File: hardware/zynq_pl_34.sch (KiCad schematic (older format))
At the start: 1 part

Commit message: Added a few Todos.
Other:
- note added: "TODO: VCCO(AFAIK 1,8 V), is VREF needed for this single ended signals?"
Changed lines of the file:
@@
 Wire Wire Line
 	5250 2200 4800 2200
+Text Notes 1650 1350 0    60   ~ 0
+TODO: VCCO(AFAIK 1,8 V), is VREF needed for this single ended signals?
 $EndSCHEMATC

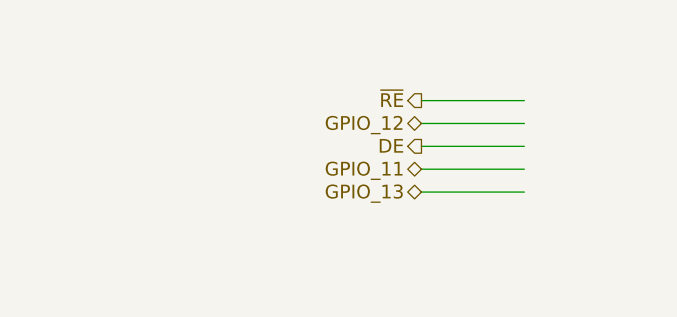
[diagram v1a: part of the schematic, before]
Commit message: Added decoupling Capacitors for the Zynq. Also added the 2,5 V Power supply.
The 2,5 V supply was implemented as LDO and is sourced by the 3,3 V Line.
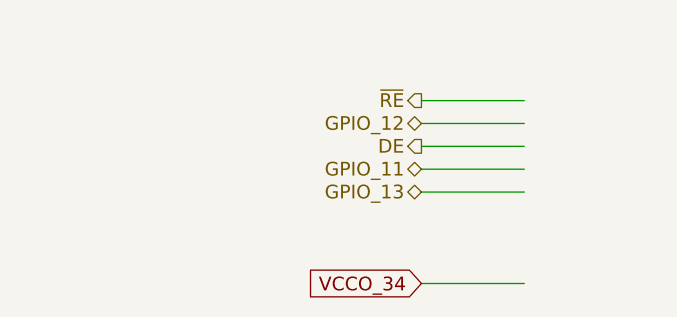
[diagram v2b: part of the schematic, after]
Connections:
- net labels added: VCCO_34
- wire segments 29 -> 30
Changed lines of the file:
@@
 Text Notes 1650 1350 0    60   ~ 0
 TODO: VCCO(AFAIK 1,8 V), is VREF needed for this single ended signals?
+Text GLabel 4800 5800 0    60   Input ~ 0
+VCCO_34
+Wire Wire Line
+	4800 5800 5250 5800
 $EndSCHEMATC

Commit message: Started to route DDR3 Memory.
At first added missing Footprint for Reference- and Terminationvoltage Regulator. Added Powerplanes for GND and VCCO. Added decoupling Network to both DDR3 Memory Chips. There are more small caps, to support Memory from other Manufactors.
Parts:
- gave numbers to parts that had none: 1
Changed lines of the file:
@@
 $EndDescr
 $Comp
-L xc7z030sbg485 U?
+L xc7z030sbg485 U1
 U 3 1 596E796D
 P 5250 800
-F 0 "U?" H 5450 1050 60  0000 L CNN
+F 0 "U1" H 5450 1050 60  0000 L CNN
 F 1 "xc7z030sbg485" H 5450 950 60  0000 L CNN
 F 2 "footprints:SBG485_22x22_19.0x19.0mm_Pitch0.8mm" H 5250 800 60  0001 C CNN

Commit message: Added Power/Protection Circuit
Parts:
- renumbered U1 to U201
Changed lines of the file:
@@
 $EndDescr
 $Comp
-L xc7z030sbg485 U1
+L xc7z030sbg485 U201
 U 3 1 596E796D
 P 5250 800
-F 0 "U1" H 5450 1050 60  0000 L CNN
+F 0 "U201" H 5450 1050 60  0000 L CNN
 F 1 "xc7z030sbg485" H 5450 950 60  0000 L CNN
 F 2 "footprints:SBG485_22x22_19.0x19.0mm_Pitch0.8mm" H 5250 800 60  0001 C CNN
